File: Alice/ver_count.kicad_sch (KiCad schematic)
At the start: 327 parts, among them Q10 NOT_OC, Q100 NOT_OC, Q101 NOT_OC, Q102 NOT_OC, Q103 NOT_OC, Q104 NOT_OC, Q105 NOT_OC, Q106 NOT_OC, Q107 NOT_OC, Q108 NOT_OC, Q109 NOT_OC, Q11 NOT_OC, Q110 NOT_OC, Q111 NOT_OC, Q112 NOT_OC, Q113 NOT_OC, Q114 NOT_OC, Q115 NOT_OC, Q116 NOT_OC, Q117 NOT_OC, Q118 NOT_OC, Q119 NOT_OC, Q12 NOT_OC, Q120 NOT_OC, Q121 NOT_OC, Q122 NOT_OC, Q123 NOT_OC, Q124 NOT_OC, Q125 NOT_OC, Q126 NOT_OC, Q127 NOT_OC, Q128 NOT_OC, Q129 NOT_OC, Q13 NOT_OC, Q130 NOT_OC, Q131 NOT_OC, Q132 NOT_OC, Q133 NOT_OC, Q134 NOT_OC, Q135 NOT_OC, Q136 NOT_OC, Q137 NOT_OC, Q138 NOT_OC, Q139 NOT_OC, Q14 NOT_OC, Q140 NOT_OC, Q141 NOT_OC, Q142 NOT_OC, Q143 NOT_OC, Q144 NOT_OC, Q145 NOT_OC, Q146 NOT_OC, Q147 NOT_OC, Q148 NOT_OC, Q149 NOT_OC, Q15 NOT_OC, Q150 NOT_OC, Q151 NOT_OC, Q152 NOT_OC, Q153 NOT_OC, Q154 NOT_OC, Q155 NOT_OC, Q156 NOT_OC, Q157 NOT_OC, Q158 NOT_OC, Q16 NOT_OC, Q17 NOT_OC, Q18 NOT_OC, Q19 NOT_OC, Q20 NOT_OC, Q21 NOT_OC, Q22 NOT_OC, Q23 NOT_OC, Q24 NOT_OC, Q25 NOT_OC, Q26 NOT_OC, Q27 NOT_OC, Q270 NOT_OC, Q271 NOT_OC, Q272 NOT_OC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

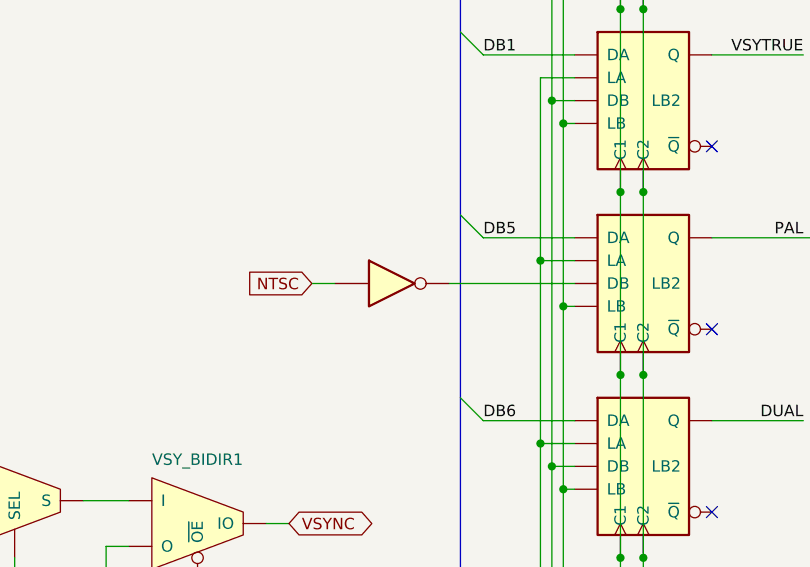
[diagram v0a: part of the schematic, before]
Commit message: Added PAL/NTSC chip option
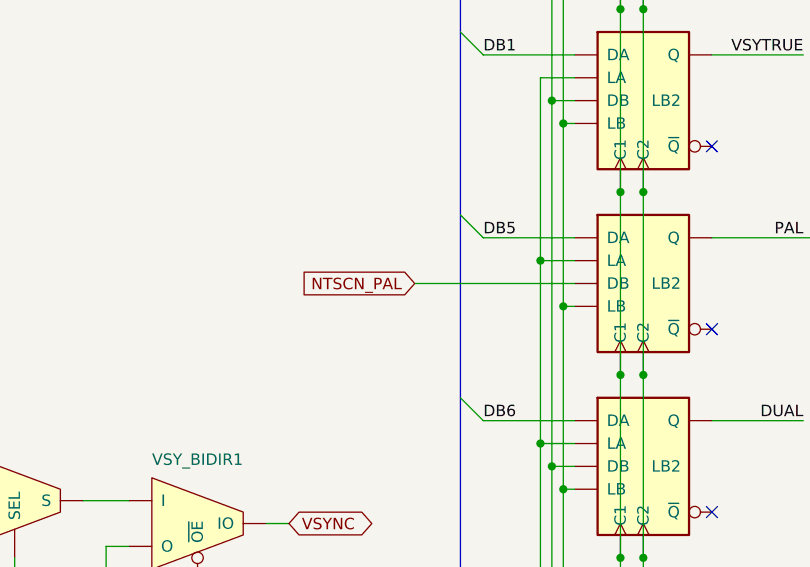
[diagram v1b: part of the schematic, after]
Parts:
- removed NOT_10: NOT, symbol NMOS:NOT
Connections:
- net NTSCN_PAL: now reaches BEAMCON0_LB5.3 (DB)
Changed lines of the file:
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@@
     (stroke (width 0) (type default) (color 0 0 0 0))
   )
-  (wire (pts (xy 401.32 259.08) (xy 403.86 259.08))
-    (stroke (width 0) (type default) (color 0 0 0 0))
-  )
   (wire (pts (xy 95.25 35.56) (xy 95.25 36.83))
     (stroke (width 0) (type default) (color 0 0 0 0))
@@
     (stroke (width 0) (type default) (color 0 0 0 0))
   )
-  (wire (pts (xy 416.56 259.08) (xy 430.53 259.08))
+  (wire (pts (xy 412.75 259.08) (xy 430.53 259.08))
     (stroke (width 0) (type default) (color 0 0 0 0))
   )
@@
     )
   )
-  (global_label "NTSC" (shape input) (at 401.32 259.08 180) (fields_autoplaced)
+  (global_label "NTSCN_PAL" (shape input) (at 412.75 259.08 180) (fields_autoplaced)
     (effects (font (size 1.27 1.27)) (justify right))
-    (property "Intersheet References" "${INTERSHEET_REFS}" (id 0) (at 394.1293 259.0006 0)
+    (property "Intersheet References" "${INTERSHEET_REFS}" (id 0) (at 399.8745 259.0006 0)
       (effects (font (size 1.27 1.27)) (justify right) hide)
     )
@@
       (effects (font (size 1.27 1.27)) hide)
     )
-    (pin "1")
-    (pin "2")
-  )
-  (symbol (lib_id "NMOS:NOT") (at 410.21 259.08 0) (unit 1)
-    (in_bom yes) (on_board yes) (fields_autoplaced)
-    (property "Reference" "NOT_10" (id 0) (at 410.21 255.27 0)
-      (effects (font (size 1.27 1.27)) hide)
-    )
-    (property "Value" "NOT" (id 1) (at 410.21 264.16 0)
-      (effects (font (size 1.27 1.27)) hide)
-    )
-    (property "Footprint" "" (id 2) (at 410.21 259.08 0)
-      (effects (font (size 1.27 1.27)) hide)
-    )
-    (property "Datasheet" "" (id 3) (at 410.21 259.08 0)
-      (effects (font (size 1.27 1.27)) hide)
-    )

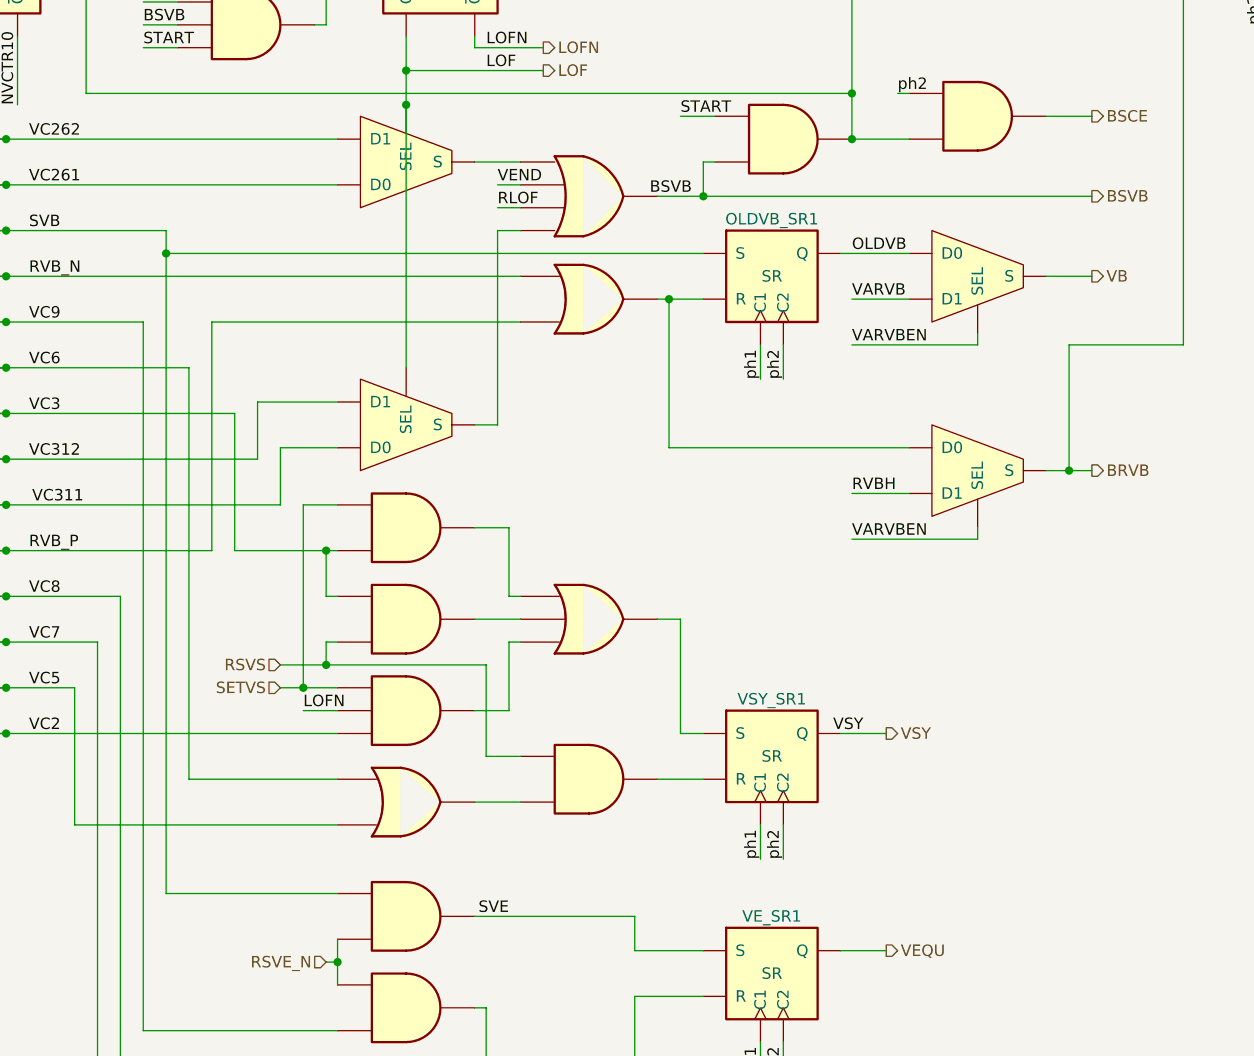
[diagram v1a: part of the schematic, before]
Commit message: Fixed synchros generation
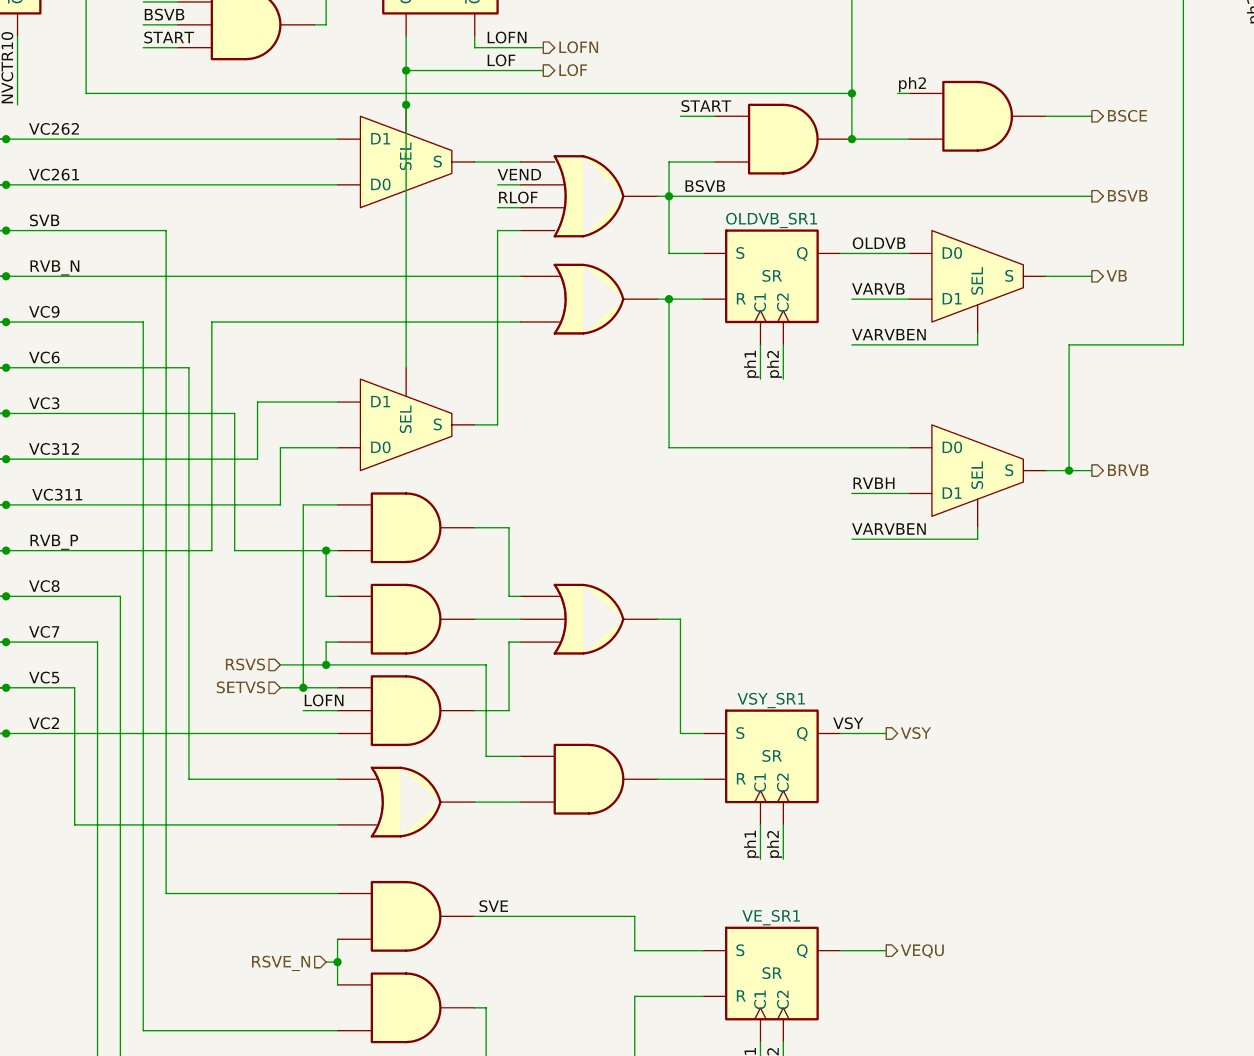
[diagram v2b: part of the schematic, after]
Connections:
- net BSVB: now also OLDVB_SR1.7 (S)
- net SVB: no longer OLDVB_SR1.7 (S)
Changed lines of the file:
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@@
   (junction (at 104.14 97.79) (diameter 0) (color 0 0 0 0)
   )
+  (junction (at 334.01 99.06) (diameter 0) (color 0 0 0 0)
+  )
   (junction (at 123.19 72.39) (diameter 0) (color 0 0 0 0)
   )
@@
   (junction (at 96.52 143.51) (diameter 0) (color 0 0 0 0)
   )
-  (junction (at 278.13 105.41) (diameter 0) (color 0 0 0 0)
-  )
   (junction (at 185.42 135.89) (diameter 0) (color 0 0 0 0)
   )
@@
   (junction (at 161.29 133.35) (diameter 0) (color 0 0 0 0)
   )
-  (junction (at 337.82 99.06) (diameter 0) (color 0 0 0 0)
-  )
   (junction (at 208.28 269.24) (diameter 0) (color 0 0 0 0)
   )
@@
     (stroke (width 0) (type default) (color 0 0 0 0))
   )
-  (wire (pts (xy 337.82 95.25) (xy 337.82 99.06))
+  (wire (pts (xy 334.01 95.25) (xy 334.01 99.06))
     (stroke (width 0) (type default) (color 0 0 0 0))
   )
@@
     (stroke (width 0) (type default) (color 0 0 0 0))
   )
-  (wire (pts (xy 278.13 105.41) (xy 337.82 105.41))
-    (stroke (width 0) (type default) (color 0 0 0 0))
-  )
   (wire (pts (xy 77.47 318.77) (xy 96.52 318.77))
     (stroke (width 0) (type default) (color 0 0 0 0))
@@
     (stroke (width 0) (type default) (color 0 0 0 0))
   )
-  (wire (pts (xy 332.74 99.06) (xy 337.82 99.06))
+  (wire (pts (xy 332.74 99.06) (xy 334.01 99.06))
     (stroke (width 0) (type default) (color 0 0 0 0))
   )
@@
     (stroke (width 0) (type default) (color 0 0 0 0))
   )
-  (wire (pts (xy 337.82 95.25) (xy 339.09 95.25))
+  (wire (pts (xy 334.01 95.25) (xy 339.09 95.25))
     (stroke (width 0) (type default) (color 0 0 0 0))
   )
@@
     (stroke (width 0) (type default) (color 0 0 0 0))
   )
+  (wire (pts (xy 334.01 105.41) (xy 334.01 99.06))
+    (stroke (width 0) (type default) (color 0 0 0 0))
+  )
   (wire (pts (xy 176.53 125.73) (xy 176.53 130.81))
     (stroke (width 0) (type default) (color 0 0 0 0))
@@
     (stroke (width 0) (type default) (color 0 0 0 0))
   )
-  (wire (pts (xy 278.13 102.87) (xy 278.13 105.41))
+  (wire (pts (xy 278.13 102.87) (xy 278.13 176.53))
     (stroke (width 0) (type default) (color 0 0 0 0))
   )
@@
     (stroke (width 0) (type default) (color 0 0 0 0))
   )
+  (wire (pts (xy 334.01 99.06) (xy 381 99.06))
+    (stroke (width 0) (type default) (color 0 0 0 0))
+  )
   (wire (pts (xy 97.79 146.05) (xy 97.79 151.13))
     (stroke (width 0) (type default) (color 0 0 0 0))
@@
     (stroke (width 0) (type default) (color 0 0 0 0))
   )
-  (wire (pts (xy 337.82 99.06) (xy 381 99.06))
+  (wire (pts (xy 337.82 105.41) (xy 334.01 105.41))
     (stroke (width 0) (type default) (color 0 0 0 0))
   )
@@
     (stroke (width 0) (type default) (color 0 0 0 0))
   )
-  (wire (pts (xy 278.13 105.41) (xy 278.13 176.53))
-    (stroke (width 0) (type default) (color 0 0 0 0))
-  )
   (wire (pts (xy 142.24 62.23) (xy 161.29 62.23))
     (stroke (width 0) (type default) (color 0 0 0 0))
@@
     (effects (font (size 1.27 1.27)) (justify left bottom))
   )
-  (label "BSVB" (at 336.55 99.06 180)
+  (label "BSVB" (at 340.36 99.06 180)
     (effects (font (size 1.27 1.27)) (justify right bottom))
   )

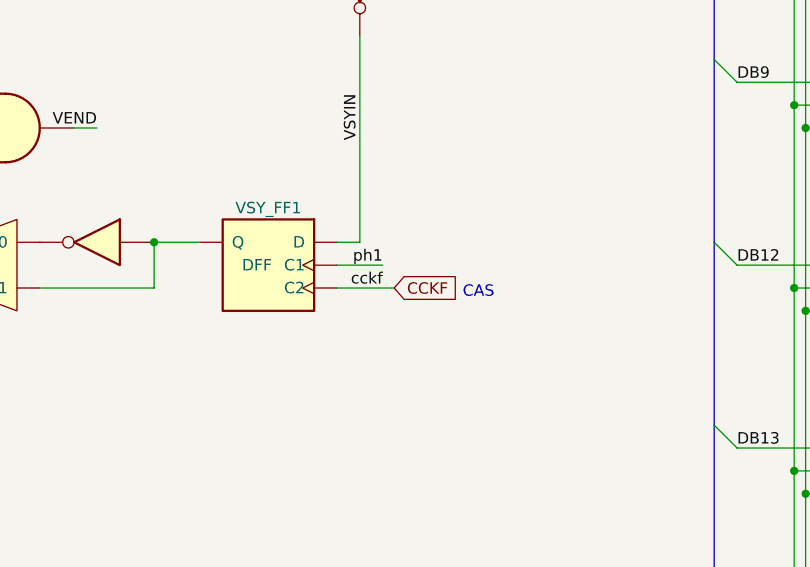
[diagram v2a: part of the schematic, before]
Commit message: Fixed CAS clock polarity, added DMA priority logic
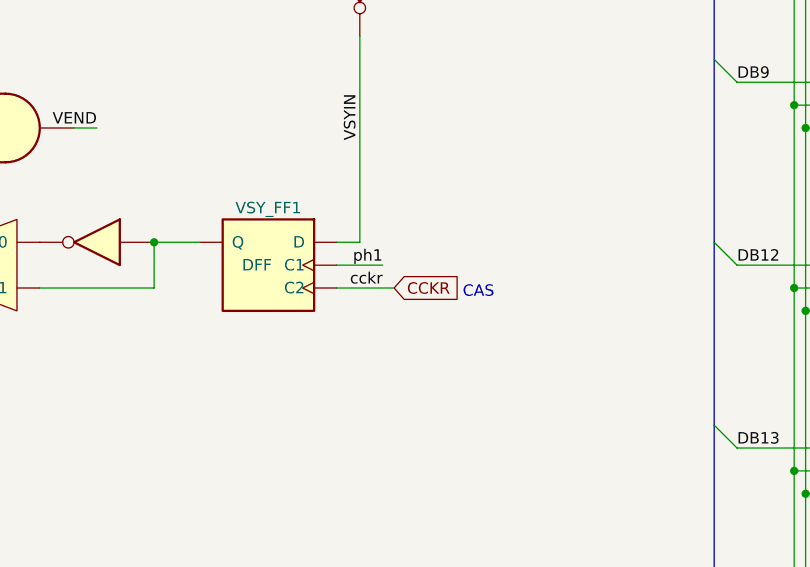
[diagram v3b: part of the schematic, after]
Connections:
- net CCKF renamed CCKR
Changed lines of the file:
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@@
     (effects (font (size 1.27 1.27)) (justify right bottom))
   )
-  (label "cckf" (at 381 337.82 180)
+  (label "cckr" (at 381 337.82 180)
     (effects (font (size 1.27 1.27)) (justify right bottom))
   )
@@
     )
   )
-  (global_label "CCKF" (shape input) (at 382.27 337.82 0) (fields_autoplaced)
+  (global_label "CCKR" (shape input) (at 382.27 337.82 0) (fields_autoplaced)
     (effects (font (size 1.27 1.27)) (justify left))
-    (property "Intersheet References" "${INTERSHEET_REFS}" (id 0) (at 389.5817 337.8994 0)
+    (property "Intersheet References" "${INTERSHEET_REFS}" (id 0) (at 389.7631 337.7406 0)
       (effects (font (size 1.27 1.27)) (justify left) hide)
     )

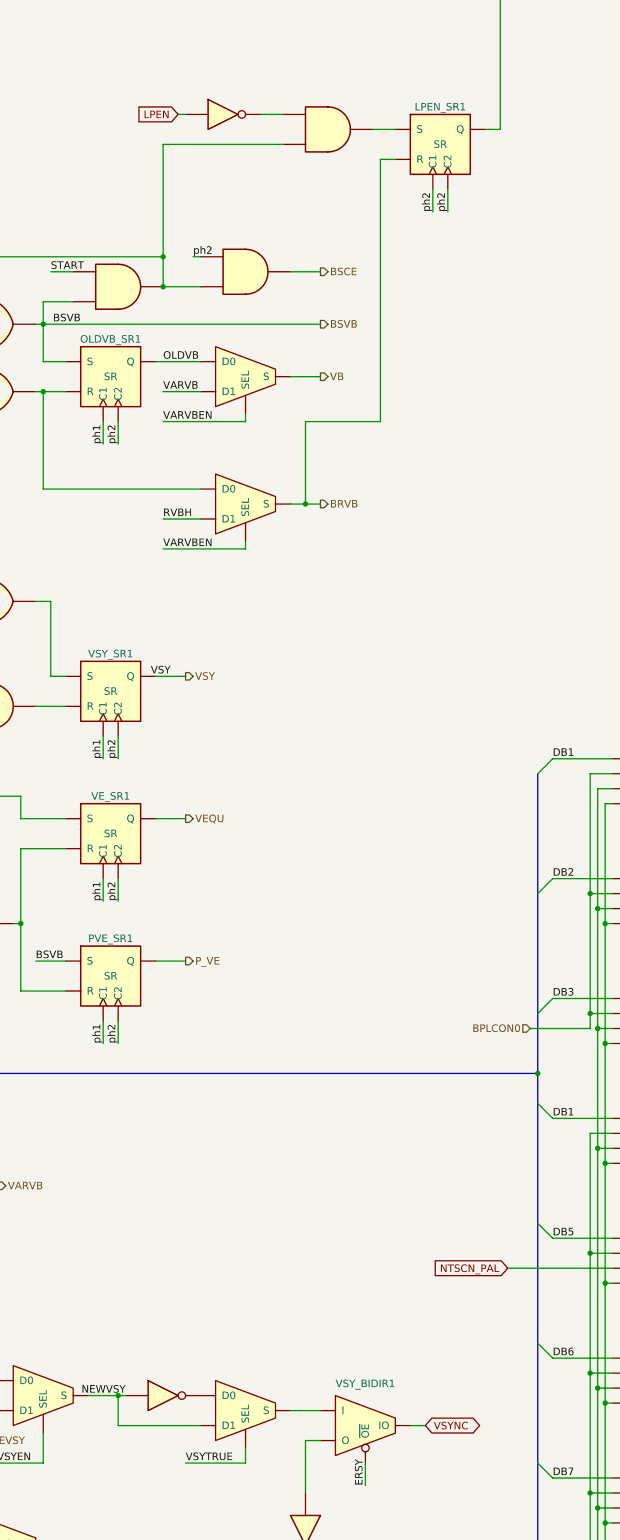
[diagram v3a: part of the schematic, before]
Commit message: RGA bus added (WIP), I/Os renamed with PAD_ prefix
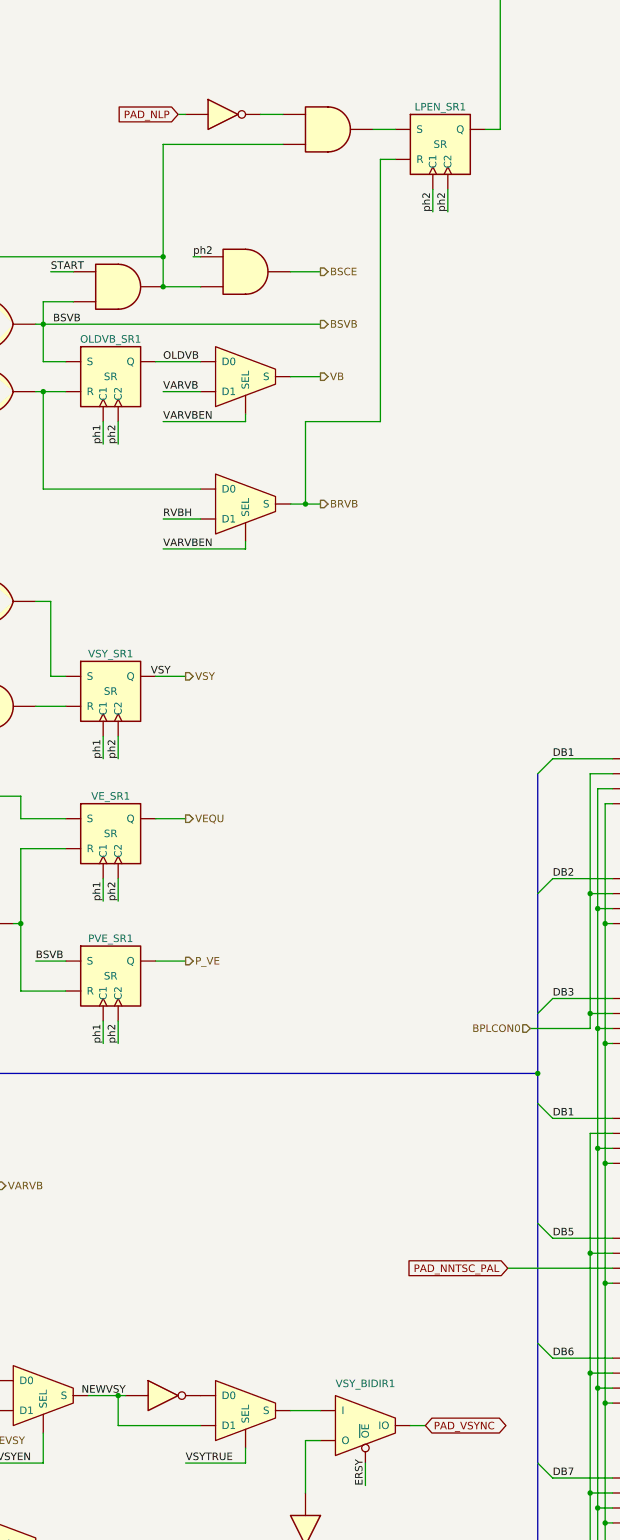
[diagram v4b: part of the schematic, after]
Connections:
- net LPEN renamed PAD_NLP
- net NTSCN_PAL renamed PAD_NNTSC_PAL
- net VSYNC renamed PAD_VSYNC
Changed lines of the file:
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@@
     )
   )
-  (global_label "VSYNC" (shape bidirectional) (at 398.78 285.75 0) (fields_autoplaced)
+  (global_label "PAD_VSYNC" (shape bidirectional) (at 398.78 285.75 0) (fields_autoplaced)
     (effects (font (size 1.27 1.27)) (justify left))
-    (property "Intersheet References" "${INTERSHEET_REFS}" (id 0) (at 407.1802 285.8294 0)
+    (property "Intersheet References" "${INTERSHEET_REFS}" (id 0) (at 411.7764 285.6706 0)
       (effects (font (size 1.27 1.27)) (justify left) hide)
     )
@@
     )
   )
-  (global_label "NTSCN_PAL" (shape input) (at 412.75 259.08 180) (fields_autoplaced)
+  (global_label "PAD_NNTSC_PAL" (shape input) (at 412.75 259.08 180) (fields_autoplaced)
     (effects (font (size 1.27 1.27)) (justify right))
-    (property "Intersheet References" "${INTERSHEET_REFS}" (id 0) (at 399.8745 259.0006 0)
+    (property "Intersheet References" "${INTERSHEET_REFS}" (id 0) (at 395.2783 259.0006 0)
       (effects (font (size 1.27 1.27)) (justify right) hide)
     )
   )
-  (global_label "LPEN" (shape input) (at 356.87 63.5 180) (fields_autoplaced)
+  (global_label "PAD_NLP" (shape input) (at 356.87 63.5 180) (fields_autoplaced)
     (effects (font (size 1.27 1.27)) (justify right))
-    (property "Intersheet References" "${INTERSHEET_REFS}" (id 0) (at 349.6793 63.4206 0)
+    (property "Intersheet References" "${INTERSHEET_REFS}" (id 0) (at 346.2321 63.4206 0)
       (effects (font (size 1.27 1.27)) (justify right) hide)
     )

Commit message: Some refactoring : BEAMCON0 and BPLCON0 moved to the top sheet, CLOCKGEN added
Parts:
- removed BEAMCON0_LB1, BEAMCON0_LB12, BEAMCON0_LB13, BEAMCON0_LB14, BEAMCON0_LB5, BEAMCON0_LB6, BEAMCON0_LB7, BEAMCON0_LB9, BPLCON0_LB1, BPLCON0_LB2, BPLCON0_LB3: LB2, symbol NMOS:LB2
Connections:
- no-connect marks 12 -> 2
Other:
- moved on the sheet: VSY_BIDIR1
